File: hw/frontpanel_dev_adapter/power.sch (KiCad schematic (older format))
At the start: 44 parts, among them J201 KLD-0202-A, J202 Conn_WR-FAST_01x04, J203 Molex_MicroFit_30-43045-0421, Q201 Si4497DY, U201 TPS54332DDA, U202 TLV1117LV30DCY, U203 TLV1117LV30DCY

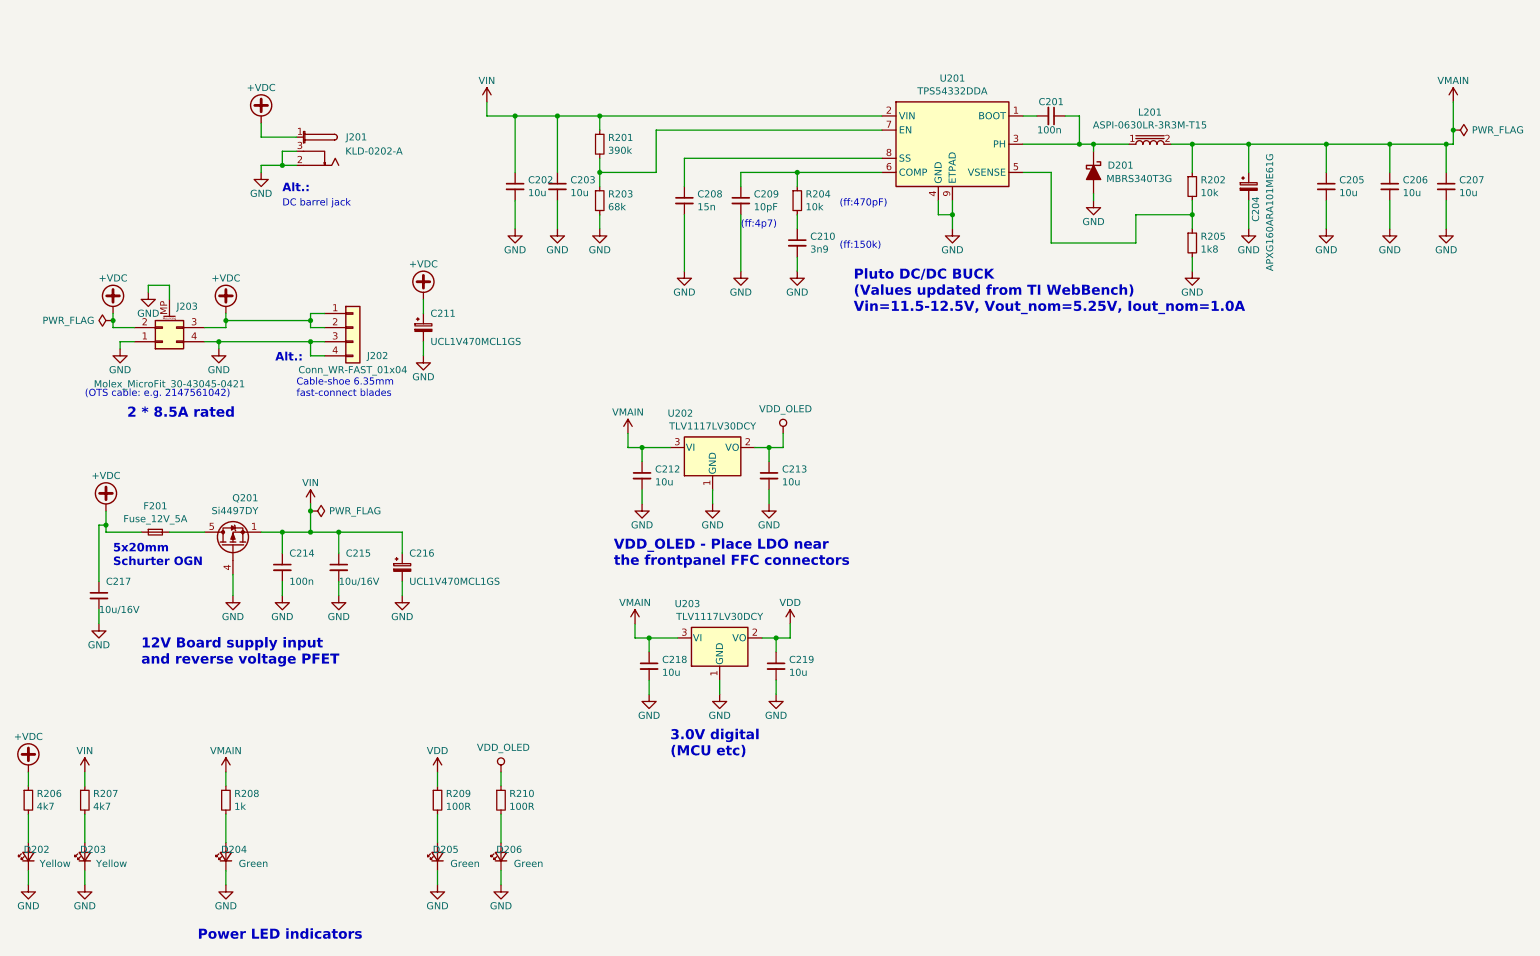
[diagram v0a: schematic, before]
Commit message: Frontpanel dev adapter: Optimize some LCSC components for JLC assembly; add some datasheets. Optimize F103 16MHz xtal routing
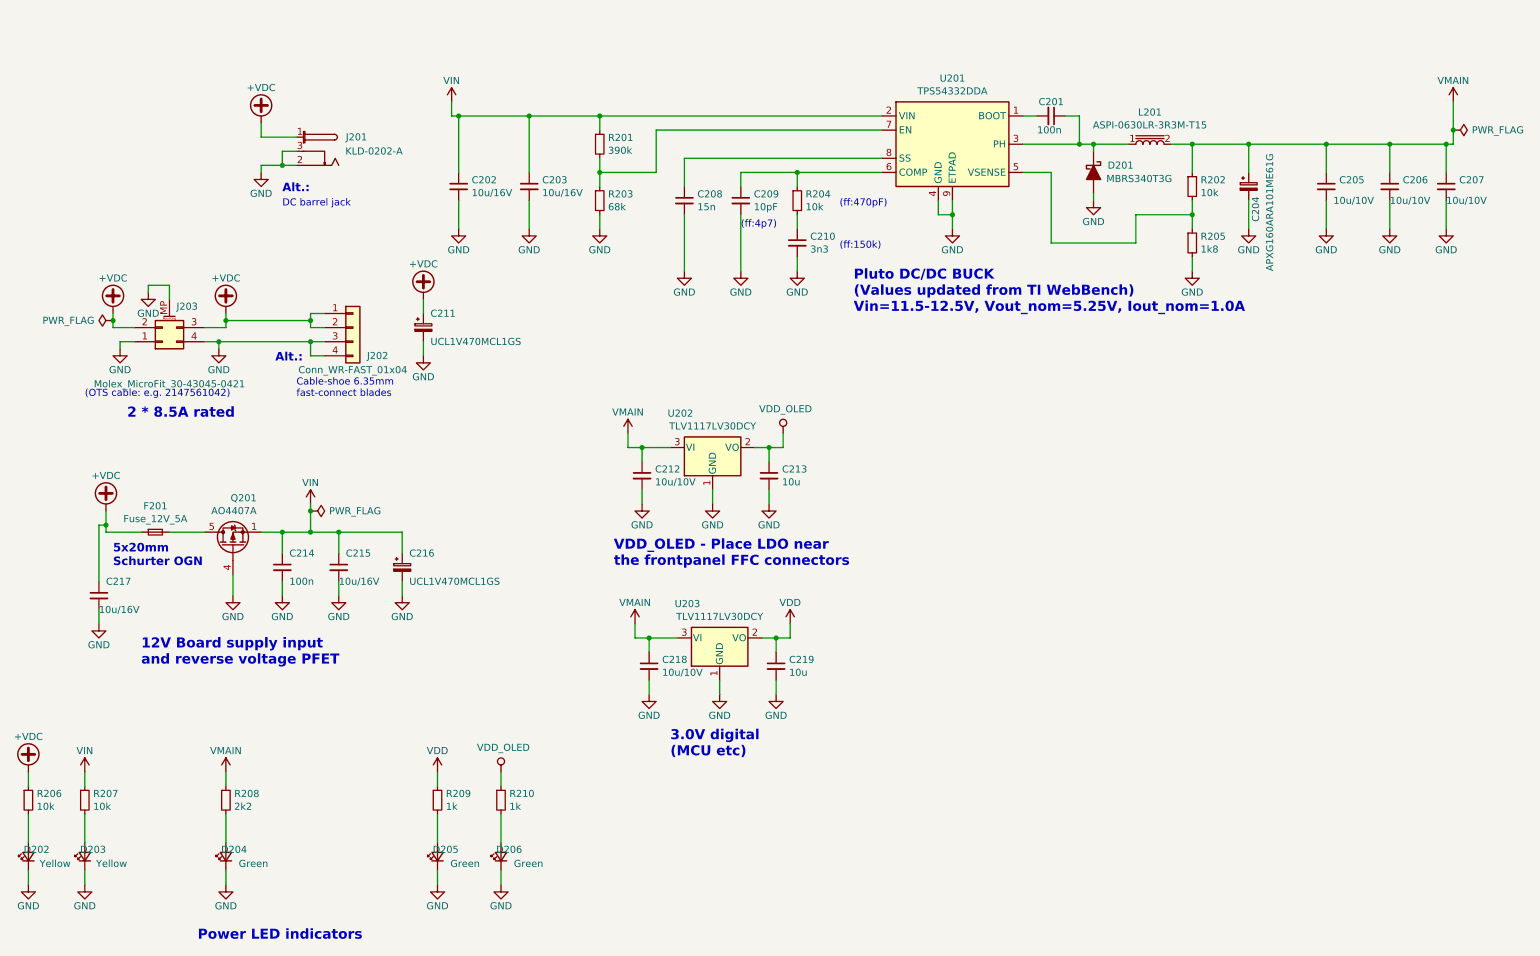
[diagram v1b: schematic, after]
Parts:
- removed Q201: Si4497DY, customlib_mj_fp:SOIC-8_3.9x4.9mm_P1.27mm, symbol customlib_mj:Si4497DY
- added Q201: AO4407A, customlib_mj_fp:SOIC-8_3.9x4.9mm_P1.27mm, symbol customlib_mj:AO4407A
- C202, C203: value 10u -> 10u/16V; footprint Capacitor_SMD:C_0603_1608Metric -> Capacitor_SMD:C_0805_2012Metric
- C205, C206, C207, C212, C218: value 10u -> 10u/10V
- C208: footprint Capacitor_SMD:C_0402_1005Metric -> Capacitor_SMD:C_0603_1608Metric
- C210: value 3n9 -> 3n3
- R202, R203, R204: footprint Resistor_SMD:R_0603_1608Metric -> Resistor_SMD:R_0402_1005Metric
- R206, R207: value 4k7 -> 10k; footprint Resistor_SMD:R_0603_1608Metric -> Resistor_SMD:R_0402_1005Metric
- R208: value 1k -> 2k2; footprint Resistor_SMD:R_0603_1608Metric -> Resistor_SMD:R_0402_1005Metric
- R209, R210: value 100R -> 1k; footprint Resistor_SMD:R_0603_1608Metric -> Resistor_SMD:R_0402_1005Metric
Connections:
- net GND: now also Q201.4 (G)
- net VIN: now also Q201.1 (S), Q201.2 (S), Q201.3 (S)
- net at F201.2: now also Q201.5 (D), Q201.6 (D), Q201.7 (D), Q201.8 (D)
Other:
- moved on the sheet: C202, C203
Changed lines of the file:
@@
 L Device:C_Small C202
 U 1 1 5F47D328
-P 4050 1950
-F 0 "C202" H 4142 1996 50  0000 L CNN
-F 1 "10u" H 4142 1905 50  0000 L CNN
-F 2 "Capacitor_SMD:C_0603_1608Metric" H 4050 1950 50  0001 C CNN
-F 3 "~" H 4050 1950 50  0001 C CNN
-	1    4050 1950
+P 3650 1950
+F 0 "C202" H 3742 1996 50  0000 L CNN
+F 1 "10u/16V" H 3742 1905 50  0000 L CNN
+F 2 "Capacitor_SMD:C_0805_2012Metric" H 3650 1950 50  0001 C CNN
+F 3 "~" H 3650 1950 50  0001 C CNN
+	1    3650 1950
 	1    0    0    -1
 $EndComp
@@
 L customlib_mj:VIN #PWR0201
 U 1 1 5F47DCB0
-P 3850 1350
-F 0 "#PWR0201" H 3850 1200 50  0001 C CNN
-F 1 "VIN" H 3850 1500 50  0000 C CNN
-F 2 "" H 3850 1350 50  0001 C CNN
-F 3 "" H 3850 1350 50  0001 C CNN
-	1    3850 1350
+P 3600 1350
+F 0 "#PWR0201" H 3600 1200 50  0001 C CNN
+F 1 "VIN" H 3600 1500 50  0000 C CNN
+F 2 "" H 3600 1350 50  0001 C CNN
+F 3 "" H 3600 1350 50  0001 C CNN
+	1    3600 1350
 	1    0    0    -1
 $EndComp
@@
 L Device:C_Small C203
 U 1 1 5F47FF6E
-P 4350 1950
-F 0 "C203" H 4442 1996 50  0000 L CNN
-F 1 "10u" H 4442 1905 50  0000 L CNN
-F 2 "Capacitor_SMD:C_0603_1608Metric" H 4350 1950 50  0001 C CNN
-F 3 "~" H 4350 1950 50  0001 C CNN
-	1    4350 1950
+P 4150 1950
+F 0 "C203" H 4242 1996 50  0000 L CNN
+F 1 "10u/16V" H 4242 1905 50  0000 L CNN
+F 2 "Capacitor_SMD:C_0805_2012Metric" H 4150 1950 50  0001 C CNN
+F 3 "~" H 4150 1950 50  0001 C CNN
+	1    4150 1950
 	1    0    0    -1
 $EndComp
@@
 F 0 "R203" H 4709 2096 50  0000 L CNN
 F 1 "68k" H 4709 2005 50  0000 L CNN
-F 2 "Resistor_SMD:R_0603_1608Metric" H 4650 2050 50  0001 C CNN
+F 2 "Resistor_SMD:R_0402_1005Metric" H 4650 2050 50  0001 C CNN
 F 3 "~" H 4650 2050 50  0001 C CNN
 	1    4650 2050
@@
 F 0 "C208" H 5342 2096 50  0000 L CNN
 F 1 "15n" H 5342 2005 50  0000 L CNN
-F 2 "Capacitor_SMD:C_0402_1005Metric" H 5250 2050 50  0001 C CNN
+F 2 "Capacitor_SMD:C_0603_1608Metric" H 5250 2050 50  0001 C CNN
 F 3 "~" H 5250 2050 50  0001 C CNN
 	1    5250 2050
@@
 F 0 "R204" H 6109 2096 50  0000 L CNN
 F 1 "10k" H 6109 2005 50  0000 L CNN
-F 2 "Resistor_SMD:R_0603_1608Metric" H 6050 2050 50  0001 C CNN
+F 2 "Resistor_SMD:R_0402_1005Metric" H 6050 2050 50  0001 C CNN
 F 3 "~" H 6050 2050 50  0001 C CNN
 	1    6050 2050
@@
 $EndComp
 Wire Wire Line
-	3850 1450 3850 1350
+	3600 1450 3600 1350
 Wire Wire Line
 	6650 1850 6050 1850
@@
 L power:GND #PWR0207
 U 1 1 5F48801F
-P 4350 2250
-F 0 "#PWR0207" H 4350 2000 50  0001 C CNN
-F 1 "GND" H 4350 2100 50  0000 C CNN
-F 2 "" H 4350 2250 50  0001 C CNN
-F 3 "" H 4350 2250 50  0001 C CNN
-	1    4350 2250
+P 4150 2250
+F 0 "#PWR0207" H 4150 2000 50  0001 C CNN
+F 1 "GND" H 4150 2100 50  0000 C CNN
+F 2 "" H 4150 2250 50  0001 C CNN
+F 3 "" H 4150 2250 50  0001 C CNN
+	1    4150 2250
 	1    0    0    -1
 $EndComp
@@
 L power:GND #PWR0206
 U 1 1 5F4882BC
-P 4050 2250
-F 0 "#PWR0206" H 4050 2000 50  0001 C CNN
-F 1 "GND" H 4050 2100 50  0000 C CNN
-F 2 "" H 4050 2250 50  0001 C CNN
-F 3 "" H 4050 2250 50  0001 C CNN
-	1    4050 2250
+P 3650 2250
+F 0 "#PWR0206" H 3650 2000 50  0001 C CNN
+F 1 "GND" H 3650 2100 50  0000 C CNN
+F 2 "" H 3650 2250 50  0001 C CNN
+F 3 "" H 3650 2250 50  0001 C CNN
+	1    3650 2250
 	1    0    0    -1
 $EndComp
@@
 Connection ~ 4650 1450
 Wire Wire Line
-	4650 1450 4350 1450
+	4650 1450 4150 1450
 Wire Wire Line
 	4650 1950 4650 1850
@@
 	4650 2250 4650 2150
 Wire Wire Line
-	4350 2250 4350 2050
-Wire Wire Line
-	4050 2250 4050 2050
-Wire Wire Line
-	4050 1850 4050 1450
-Connection ~ 4050 1450
-Wire Wire Line
-	4050 1450 3850 1450
-Wire Wire Line
-	4350 1850 4350 1450
-Connection ~ 4350 1450
-Wire Wire Line
-	4350 1450 4050 1450
+	4150 2250 4150 2050
+Wire Wire Line
+	3650 2250 3650 2050
+Wire Wire Line
+	3650 1850 3650 1450
+Connection ~ 3650 1450
+Wire Wire Line
+	3650 1450 3600 1450
+Wire Wire Line
+	4150 1850 4150 1450
+Connection ~ 4150 1450
+Wire Wire Line
+	4150 1450 3650 1450
 Wire Wire Line
 	4650 1850 5050 1850
@@
 F 0 "R202" H 8909 1996 50  0000 L CNN
 F 1 "10k" H 8909 1905 50  0000 L CNN
-F 2 "Resistor_SMD:R_0603_1608Metric" H 8850 1950 50  0001 C CNN
+F 2 "Resistor_SMD:R_0402_1005Metric" H 8850 1950 50  0001 C CNN
 F 3 "~" H 8850 1950 50  0001 C CNN
 	1    8850 1950
@@
 P 9800 1950
 F 0 "C205" H 9892 1996 50  0000 L CNN
-F 1 "10u" H 9892 1905 50  0000 L CNN
+F 1 "10u/10V" H 9850 1850 50  0000 L CNN
 F 2 "Capacitor_SMD:C_0603_1608Metric" H 9800 1950 50  0001 C CNN
 F 3 "~" H 9800 1950 50  0001 C CNN
@@
 P 5000 5350
 F 0 "C218" H 5092 5396 50  0000 L CNN
-F 1 "10u" H 5092 5305 50  0000 L CNN
+F 1 "10u/10V" H 5092 5305 50  0000 L CNN
 F 2 "Capacitor_SMD:C_0603_1608Metric" H 5000 5350 50  0001 C CNN
 F 3 "~" H 5000 5350 50  0001 C CNN
@@
 P 1000 6300
 F 0 "R207" H 1059 6346 50  0000 L CNN
-F 1 "4k7" H 1059 6255 50  0000 L CNN
-F 2 "Resistor_SMD:R_0603_1608Metric" H 1000 6300 50  0001 C CNN
+F 1 "10k" H 1059 6255 50  0000 L CNN
+F 2 "Resistor_SMD:R_0402_1005Metric" H 1000 6300 50  0001 C CNN
 F 3 "~" H 1000 6300 50  0001 C CNN
 	1    1000 6300
@@
 P 2000 6300
 F 0 "R208" H 2059 6346 50  0000 L CNN
-F 1 "1k" H 2059 6255 50  0000 L CNN
-F 2 "Resistor_SMD:R_0603_1608Metric" H 2000 6300 50  0001 C CNN
+F 1 "2k2" H 2059 6255 50  0000 L CNN
+F 2 "Resistor_SMD:R_0402_1005Metric" H 2000 6300 50  0001 C CNN
 F 3 "~" H 2000 6300 50  0001 C CNN
 	1    2000 6300
@@
 P 3500 6300
 F 0 "R209" H 3559 6346 50  0000 L CNN
-F 1 "100R" H 3559 6255 50  0000 L CNN
-F 2 "Resistor_SMD:R_0603_1608Metric" H 3500 6300 50  0001 C CNN
+F 1 "1k" H 3559 6255 50  0000 L CNN
+F 2 "Resistor_SMD:R_0402_1005Metric" H 3500 6300 50  0001 C CNN
 F 3 "~" H 3500 6300 50  0001 C CNN
 	1    3500 6300
@@
 P 4950 4000
 F 0 "C212" H 5042 4046 50  0000 L CNN
-F 1 "10u" H 5042 3955 50  0000 L CNN
+F 1 "10u/10V" H 5042 3955 50  0000 L CNN
 F 2 "Capacitor_SMD:C_0603_1608Metric" H 4950 4000 50  0001 C CNN
 F 3 "~" H 4950 4000 50  0001 C CNN
@@
 P 3950 6300
 F 0 "R210" H 4009 6346 50  0000 L CNN
-F 1 "100R" H 4009 6255 50  0000 L CNN
-F 2 "Resistor_SMD:R_0603_1608Metric" H 3950 6300 50  0001 C CNN
+F 1 "1k" H 4009 6255 50  0000 L CNN
+F 2 "Resistor_SMD:R_0402_1005Metric" H 3950 6300 50  0001 C CNN
 F 3 "~" H 3950 6300 50  0001 C CNN
 	1    3950 6300
@@
 3.0V digital\n(MCU etc)
 $Comp
-L customlib_mj:Si4497DY Q201
-U 1 1 5F6AC6C1
-P 2050 4500
-F 0 "Q201" V 2392 4320 50  0000 L CNN
-F 1 "Si4497DY" V 2301 4320 50  0000 L CNN
-F 2 "customlib_mj_fp:SOIC-8_3.9x4.9mm_P1.27mm" H 2250 4425 50  0001 L CIN
-F 3 "https://www.vishay.com/docs/65748/si4497dy.pdf" H 2050 4500 50  0001 L CNN
-	1    2050 4500
-	0    -1   -1   0
-$EndComp
-$Comp
 L power:+VDC #PWR0231
 U 1 1 5F6AF81A
@@
 P 6050 2350
 F 0 "C210" H 6142 2396 50  0000 L CNN
-F 1 "3n9" H 6142 2305 50  0000 L CNN
+F 1 "3n3" H 6142 2305 50  0000 L CNN
 F 2 "Capacitor_SMD:C_0402_1005Metric" H 6050 2350 50  0001 C CNN
 F 3 "~" H 6050 2350 50  0001 C CNN
@@
 P 10250 1950
 F 0 "C206" H 10342 1996 50  0000 L CNN
-F 1 "10u" H 10342 1905 50  0000 L CNN
+F 1 "10u/10V" H 10250 1850 50  0000 L CNN
 F 2 "Capacitor_SMD:C_0603_1608Metric" H 10250 1950 50  0001 C CNN
 F 3 "~" H 10250 1950 50  0001 C CNN
@@
 P 10650 1950
 F 0 "C207" H 10742 1996 50  0000 L CNN
-F 1 "10u" H 10742 1905 50  0000 L CNN
+F 1 "10u/10V" H 10650 1850 50  0000 L CNN
 F 2 "Capacitor_SMD:C_0603_1608Metric" H 10650 1950 50  0001 C CNN
 F 3 "~" H 10650 1950 50  0001 C CNN
@@
 P 600 6300
 F 0 "R206" H 659 6346 50  0000 L CNN
-F 1 "4k7" H 659 6255 50  0000 L CNN
-F 2 "Resistor_SMD:R_0603_1608Metric" H 600 6300 50  0001 C CNN
+F 1 "10k" H 659 6255 50  0000 L CNN
+F 2 "Resistor_SMD:R_0402_1005Metric" H 600 6300 50  0001 C CNN
 F 3 "~" H 600 6300 50  0001 C CNN
 	1    600  6300
@@
 Text Notes 2400 2100 0    50   ~ 0
 DC barrel jack
+$Comp
+L customlib_mj:AO4407A Q201
+U 1 1 60233277
+P 2050 4500
+F 0 "Q201" V 2392 4332 50  0000 L CNN
+F 1 "AO4407A" V 2301 4332 50  0000 L CNN
+F 2 "customlib_mj_fp:SOIC-8_3.9x4.9mm_P1.27mm" H 2250 4425 50  0001 L CIN
+F 3 "https://datasheet.lcsc.com/szlcsc/Alpha-Omega-Semicon-AOS-AO4407A_C16072.pdf" H 2050 4500 50  0001 L CNN
+	1    2050 4500
+	0    -1   -1   0
+$EndComp
 $EndSCHEMATC

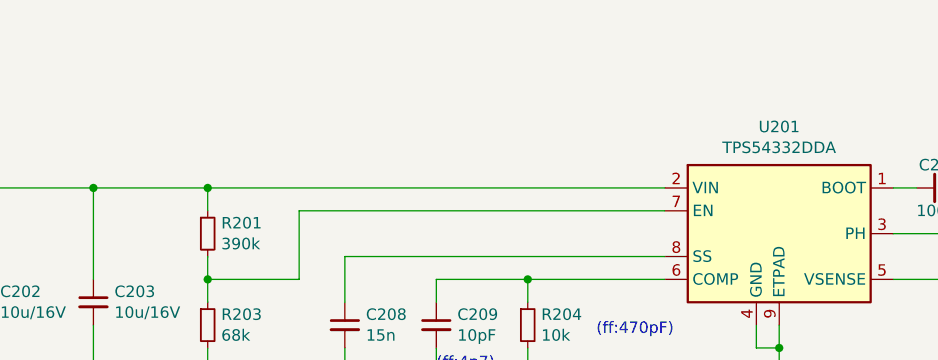
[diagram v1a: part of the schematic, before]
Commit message: FP adapter/dev board: *routing DONE* ; minor pinout tweaks (optimize routing); fix some missing 3d models
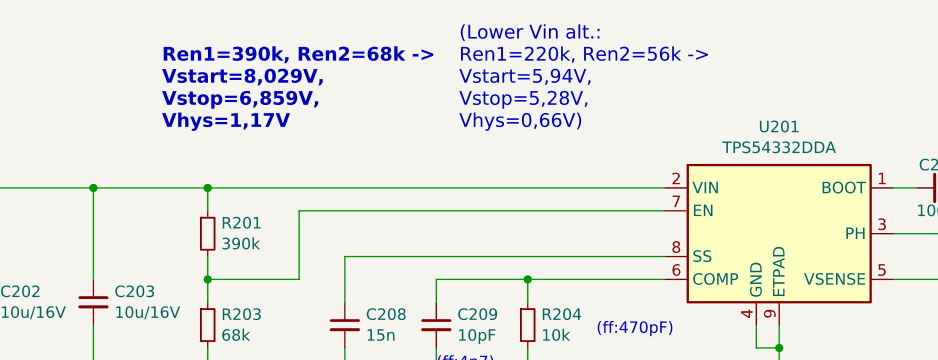
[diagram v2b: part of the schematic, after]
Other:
- note added: "(Lower Vin alt.: \nRen1=220k, Ren2=56k ->\nVstart=5,94V,\nVstop=5,28V,\nVhys=0,66V)"
- note added: "Ren1=390k, Ren2=68k ->\nVstart=8,029V,\nVstop=6,859V,\nVhys=1,17V"
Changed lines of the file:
@@
 	0    -1   -1   0
 $EndComp
+Text Notes 4450 1200 0    60   ~ 12
+Ren1=390k, Ren2=68k ->\nVstart=8,029V,\nVstop=6,859V,\nVhys=1,17V
+Text Notes 5750 1200 0    60   ~ 0
+(Lower Vin alt.: \nRen1=220k, Ren2=56k ->\nVstart=5,94V,\nVstop=5,28V,\nVhys=0,66V)
 $EndSCHEMATC
